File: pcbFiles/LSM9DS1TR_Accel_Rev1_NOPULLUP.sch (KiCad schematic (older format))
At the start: 8 parts

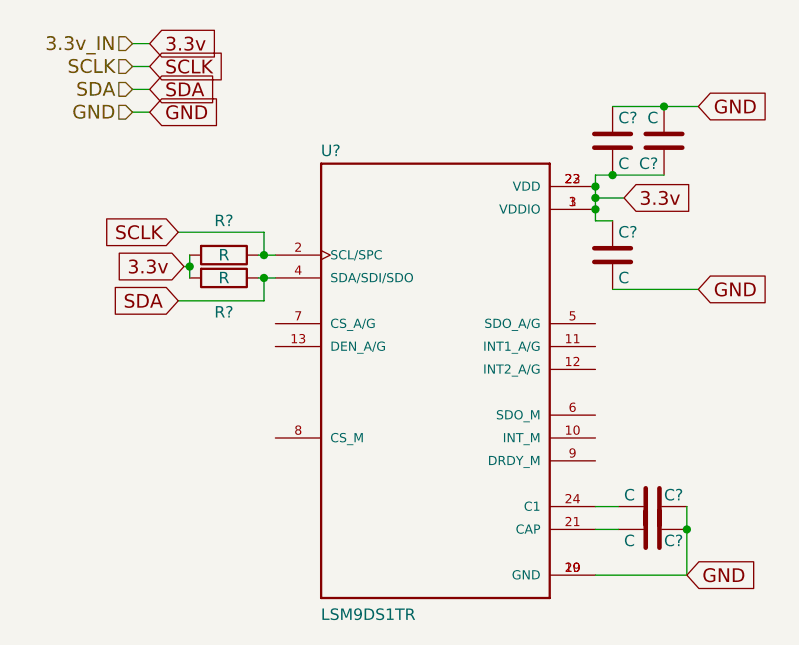
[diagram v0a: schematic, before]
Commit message: Update the circuit schematic
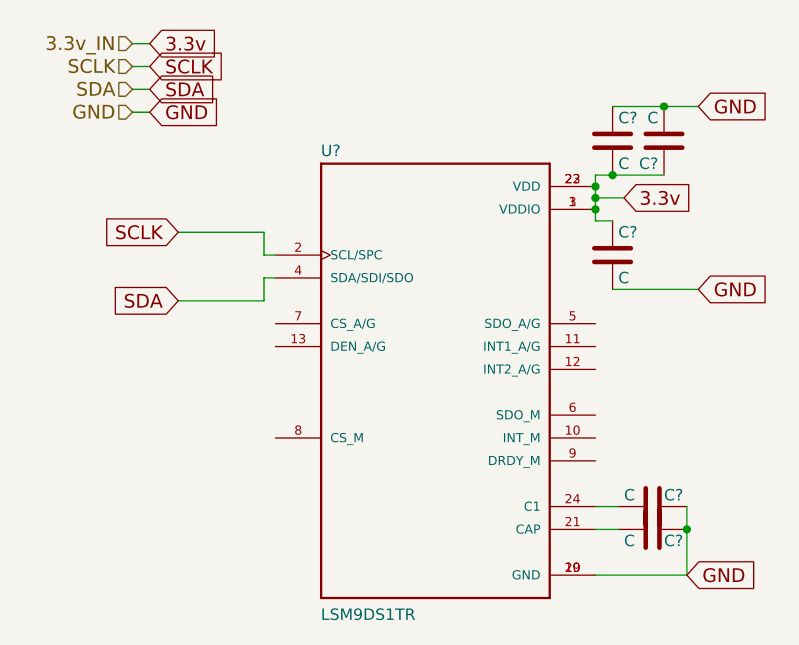
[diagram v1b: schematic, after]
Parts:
- removed R? (x2): R, symbol R
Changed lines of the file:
@@
 $Descr A4 11693 8268
 encoding utf-8
-Sheet 5 7
+Sheet 6 12
 Title ""
 Date ""
@@
 U 1 1 5C4A2352
 P 5375 3325
+AR Path="/5C4A2290/5C4A2352" Ref="U?"  Part="1"
+AR Path="/5C4A8BAE/5C4A2352" Ref="U?"  Part="1"
 F 0 "U?" H 4874 4352 50  0000 L BNN
 F 1 "LSM9DS1TR" H 4874 2323 50  0000 L BNN
@@
 U 1 1 5C4A23DC
 P 6325 3825
+AR Path="/5C4A2290/5C4A23DC" Ref="C?"  Part="1"
+AR Path="/5C4A8BAE/5C4A23DC" Ref="C?"  Part="1"
 F 0 "C?" V 6275 3875 50  0000 L CNN
 F 1 "C" V 6275 3700 50  0000 L CNN
@@
 U 1 1 5C4A24C3
 P 6325 3925
+AR Path="/5C4A2290/5C4A24C3" Ref="C?"  Part="1"
+AR Path="/5C4A8BAE/5C4A24C3" Ref="C?"  Part="1"
 F 0 "C?" V 6375 3975 50  0000 L CNN
 F 1 "C" V 6375 3800 50  0000 L CNN
@@
 U 1 1 5C4A251C
 P 6150 2225
+AR Path="/5C4A2290/5C4A251C" Ref="C?"  Part="1"
+AR Path="/5C4A8BAE/5C4A251C" Ref="C?"  Part="1"
 F 0 "C?" H 6175 2325 50  0000 L CNN
 F 1 "C" H 6175 2125 50  0000 L CNN
@@
 U 1 1 5C4A258F
 P 6375 2225
+AR Path="/5C4A2290/5C4A258F" Ref="C?"  Part="1"
+AR Path="/5C4A8BAE/5C4A258F" Ref="C?"  Part="1"
 F 0 "C?" H 6400 2325 50  0000 L CNN
 F 1 "C" H 6400 2125 50  0000 L CNN
@@
 U 1 1 5C4A25B2
 P 6150 2725
+AR Path="/5C4A2290/5C4A25B2" Ref="C?"  Part="1"
+AR Path="/5C4A8BAE/5C4A25B2" Ref="C?"  Part="1"
 F 0 "C?" H 6175 2825 50  0000 L CNN
 F 1 "C" H 6175 2625 50  0000 L CNN
@@
 	1    0    0    -1
 $EndComp
-$Comp
-L R R?
-U 1 1 5C4A26D9
-P 4450 2725
-F 0 "R?" V 4300 2725 50  0000 C CNN
-F 1 "R" V 4450 2725 50  0000 C CNN
-F 2 "" V 4380 2725 50  0001 C CNN
-F 3 "" H 4450 2725 50  0001 C CNN
-	1    4450 2725
-	0    1    1    0
-$EndComp
-$Comp
-L R R?
-U 1 1 5C4A2742
-P 4450 2825
-F 0 "R?" V 4600 2825 50  0000 C CNN
-F 1 "R" V 4450 2825 50  0000 C CNN
-F 2 "" V 4380 2825 50  0001 C CNN
-F 3 "" H 4450 2825 50  0001 C CNN
-	1    4450 2825
-	0    1    1    0
-$EndComp
-Text GLabel 4275 2775 0    60   Input ~ 0
-3.3v
-Wire Wire Line
-	4300 2725 4300 2825
-Wire Wire Line
-	4300 2775 4275 2775
-Connection ~ 4300 2775
-Wire Wire Line
-	4600 2725 4675 2725
-Wire Wire Line
-	4675 2825 4600 2825
 Text GLabel 4250 2925 0    60   Input ~ 0
 SDA
@@
 Wire Wire Line
 	4625 2625 4625 2725
-Connection ~ 4625 2725
 Wire Wire Line
 	4625 2825 4625 2925
 Wire Wire Line
 	4625 2925 4250 2925
-Connection ~ 4625 2825
 Text GLabel 6200 2475 2    60   Input ~ 0
 3.3v
@@
 Wire Wire Line
 	4125 2100 4050 2100
+Wire Wire Line
+	4625 2725 4675 2725
+Wire Wire Line
+	4625 2825 4675 2825
 $EndSCHEMATC

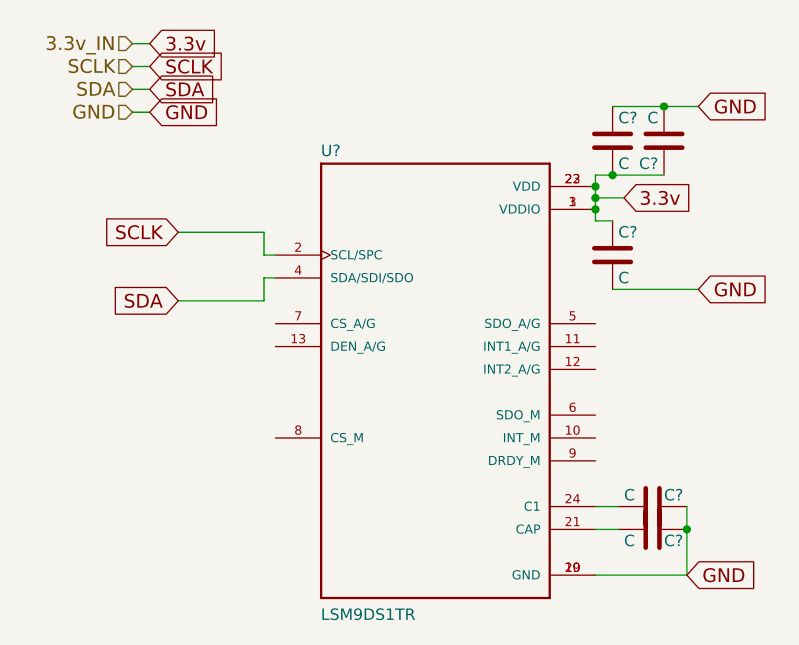
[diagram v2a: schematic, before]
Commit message: Update Footprints and Board Layers
Still need to get foorprint for x... device and the lpf may need to make them if I cannot find them @willcarroll7
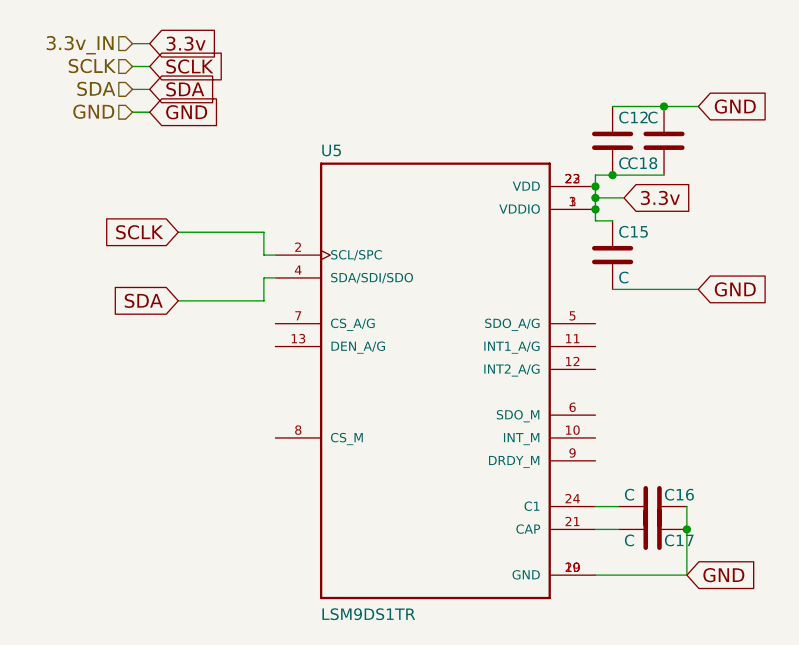
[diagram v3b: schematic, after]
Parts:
- removed C? (x2): C, symbol C
- removed U?: LSM9DS1TR, PQFN43P300X350X102-24N, symbol LSM9DS1TR
- added C15, C17: C, Capacitors_SMD:C_0402, symbol C
- added U5: LSM9DS1TR, LSM9DS1TR:PQFN43P300X350X102-24N, symbol LSM9DS1TR
- C12, C16, C18: renamed from C?; footprint (none) -> Capacitors_SMD:C_0402
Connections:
- net 3.3v: now also C15.1, U5.1 (VDDIO), U5.22 (VDD), U5.23 (VDD), U5.3 (VDDIO)
- net GND: now also C15.2, C17.1, U5.19 (GND), U5.20 (GND)
- net SCLK: now also U5.2 (SCL/SPC)
- net SDA: now also U5.4 (SDA/SDI/SDO)
- net at C16.2: now also U5.24 (C1)
- new net: C17.2, U5.21 (CAP)
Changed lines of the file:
@@
-EESchema Schematic File Version 4
+EESchema Schematic File Version 2
 LIBS:power
+LIBS:device
+LIBS:switches
+LIBS:relays
+LIBS:motors
+LIBS:transistors
+LIBS:conn
+LIBS:linear
+LIBS:regul
 LIBS:74xx
+LIBS:cmos4000
+LIBS:adc-dac
+LIBS:memory
+LIBS:xilinx
+LIBS:microcontrollers
+LIBS:dsp
+LIBS:microchip
+LIBS:analog_switches
+LIBS:motorola
+LIBS:texas
+LIBS:intel
+LIBS:audio
+LIBS:interface
+LIBS:digital-audio
+LIBS:philips
+LIBS:display
+LIBS:cypress
+LIBS:siliconi
+LIBS:opto
+LIBS:atmel
+LIBS:contrib
+LIBS:valves
+LIBS:ADS1115IDGST
+LIBS:CYW20719B1KUMLG
+LIBS:LSM9DS1TR
+LIBS:TPS63001DRCT
+LIBS:MCP73831T-2ACI_OT
+LIBS:A-1JB
+LIBS:XC6119N16A7R-G
 LIBS:GolfGloveMainBoardV1.0.0-cache
-EELAYER 26 0
+EELAYER 25 0
 EELAYER END
 $Descr A4 11693 8268
@@
 $Comp
 L LSM9DS1TR U?
-U 1 1 5C4A2352
+U 1 1 5C59A358
 P 5375 3325
-AR Path="/5C4A2290/5C4A2352" Ref="U?"  Part="1"
-AR Path="/5C4A8BAE/5C4A2352" Ref="U?"  Part="1"
-F 0 "U?" H 4874 4352 50  0000 L BNN
+AR Path="/5C4A2290/5C59A358" Ref="U?"  Part="1"
+AR Path="/5C4A8BAE/5C59A358" Ref="U5"  Part="1"
+F 0 "U5" H 4874 4352 50  0000 L BNN
 F 1 "LSM9DS1TR" H 4874 2323 50  0000 L BNN
-F 2 "PQFN43P300X350X102-24N" H 5375 3325 50  0001 L BNN
+F 2 "LSM9DS1TR:PQFN43P300X350X102-24N" H 5375 3325 50  0001 L BNN
 F 3 "TFLGA-24 STMicroelectronics" H 5375 3325 50  0001 L BNN
 F 4 "LSM9DS1TR" H 5375 3325 50  0001 L BNN "Field4"
@@
 P 6325 3825
 AR Path="/5C4A2290/5C4A23DC" Ref="C?"  Part="1"
-AR Path="/5C4A8BAE/5C4A23DC" Ref="C?"  Part="1"
-F 0 "C?" V 6275 3875 50  0000 L CNN
+AR Path="/5C4A8BAE/5C4A23DC" Ref="C16"  Part="1"
+F 0 "C16" V 6275 3875 50  0000 L CNN
 F 1 "C" V 6275 3700 50  0000 L CNN
-F 2 "" H 6363 3675 50  0001 C CNN
+F 2 "Capacitors_SMD:C_0402" H 6363 3675 50  0001 C CNN
 F 3 "" H 6325 3825 50  0001 C CNN
 	1    6325 3825
@@
 $Comp
 L C C?
-U 1 1 5C4A24C3
+U 1 1 5C59A35A
 P 6325 3925
-AR Path="/5C4A2290/5C4A24C3" Ref="C?"  Part="1"
-AR Path="/5C4A8BAE/5C4A24C3" Ref="C?"  Part="1"
-F 0 "C?" V 6375 3975 50  0000 L CNN
+AR Path="/5C4A2290/5C59A35A" Ref="C?"  Part="1"
+AR Path="/5C4A8BAE/5C59A35A" Ref="C17"  Part="1"
+F 0 "C17" V 6375 3975 50  0000 L CNN
 F 1 "C" V 6375 3800 50  0000 L CNN
-F 2 "" H 6363 3775 50  0001 C CNN
+F 2 "Capacitors_SMD:C_0402" H 6363 3775 50  0001 C CNN
 F 3 "" H 6325 3925 50  0001 C CNN
 	1    6325 3925
@@
 P 6150 2225
 AR Path="/5C4A2290/5C4A251C" Ref="C?"  Part="1"
-AR Path="/5C4A8BAE/5C4A251C" Ref="C?"  Part="1"
-F 0 "C?" H 6175 2325 50  0000 L CNN
+AR Path="/5C4A8BAE/5C4A251C" Ref="C12"  Part="1"
+F 0 "C12" H 6175 2325 50  0000 L CNN
 F 1 "C" H 6175 2125 50  0000 L CNN
-F 2 "" H 6188 2075 50  0001 C CNN
+F 2 "Capacitors_SMD:C_0402" H 6188 2075 50  0001 C CNN
 F 3 "" H 6150 2225 50  0001 C CNN
 	1    6150 2225
@@
 P 6375 2225
 AR Path="/5C4A2290/5C4A258F" Ref="C?"  Part="1"
-AR Path="/5C4A8BAE/5C4A258F" Ref="C?"  Part="1"
-F 0 "C?" H 6400 2325 50  0000 L CNN
+AR Path="/5C4A8BAE/5C4A258F" Ref="C18"  Part="1"
+F 0 "C18" H 6400 2325 50  0000 L CNN
 F 1 "C" H 6400 2125 50  0000 L CNN
-F 2 "" H 6413 2075 50  0001 C CNN
+F 2 "Capacitors_SMD:C_0402" H 6413 2075 50  0001 C CNN
 F 3 "" H 6375 2225 50  0001 C CNN
 	1    6375 2225
@@
 $Comp
 L C C?
-U 1 1 5C4A25B2
+U 1 1 5C59A35D
 P 6150 2725
-AR Path="/5C4A2290/5C4A25B2" Ref="C?"  Part="1"
-AR Path="/5C4A8BAE/5C4A25B2" Ref="C?"  Part="1"
-F 0 "C?" H 6175 2825 50  0000 L CNN
+AR Path="/5C4A2290/5C59A35D" Ref="C?"  Part="1"
+AR Path="/5C4A8BAE/5C59A35D" Ref="C15"  Part="1"
+F 0 "C15" H 6175 2825 50  0000 L CNN
 F 1 "C" H 6175 2625 50  0000 L CNN
-F 2 "" H 6188 2575 50  0001 C CNN
+F 2 "Capacitors_SMD:C_0402" H 6188 2575 50  0001 C CNN
 F 3 "" H 6150 2725 50  0001 C CNN
 	1    6150 2725

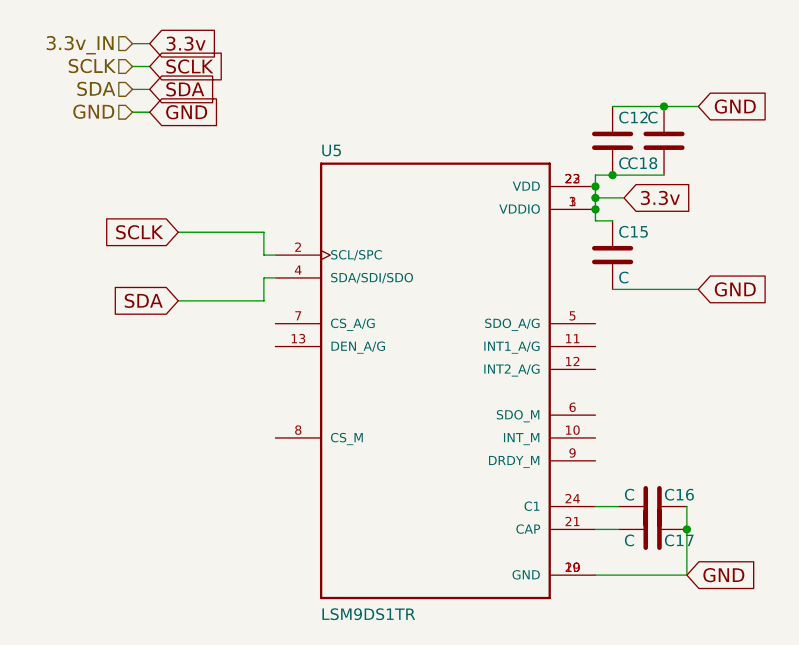
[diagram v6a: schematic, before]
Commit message: Update Board Files
Updated schematic files, completed REV1.0 of the board design, waiting for review by @willcarroll7
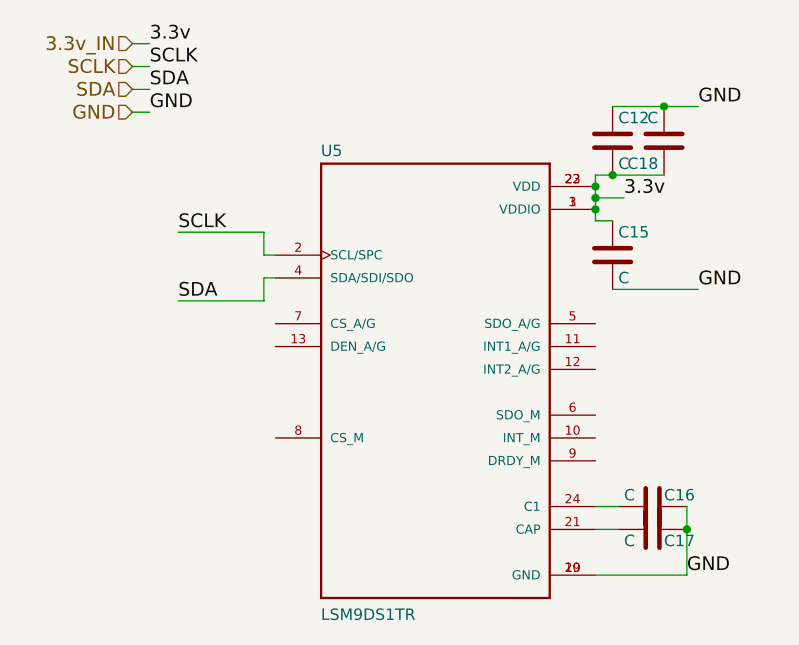
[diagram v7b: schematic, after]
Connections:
- net 3.3v renamed 3.3v_IN
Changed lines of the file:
@@
 LIBS:contrib
 LIBS:valves
-LIBS:2450AT42B100E
-LIBS:A-1JB
 LIBS:ADS1115IDGST
-LIBS:CD4011BM96
 LIBS:CYW20719B1KUMLG
 LIBS:LSM9DS1TR
+LIBS:TPS63001DRCT
 LIBS:MCP73831T-2ACI_OT
+LIBS:A-1JB
+LIBS:XC6119N16A7R-G
+LIBS:2450AT42B100E
+LIBS:CD4011BM96
 LIBS:MMDT3904V-7
 LIBS:MMPQ3904
 LIBS:S2B-PH-K-S_LF__SN_
-LIBS:TPS63001DRCT
-LIBS:XC6119N16A7R-G
 LIBS:GolfGloveMainBoardV1.0.0-cache
 EELAYER 25 0
@@
 	1    0    0    -1
 $EndComp
-Text GLabel 4250 2925 0    60   Input ~ 0
-SDA
-Text GLabel 4250 2625 0    60   Input ~ 0
-SCLK
 Wire Wire Line
 	4250 2625 4625 2625
@@
 Wire Wire Line
 	4625 2925 4250 2925
-Text GLabel 6200 2475 2    60   Input ~ 0
-3.3v
 Wire Wire Line
 	6075 2375 6075 2575
@@
 	6075 2575 6150 2575
 Connection ~ 6075 2525
-Text GLabel 6525 2075 2    60   Input ~ 0
-GND
-Text GLabel 6525 2875 2    60   Input ~ 0
-GND
 Wire Wire Line
 	6150 2075 6525 2075
@@
 Wire Wire Line
 	6150 2875 6525 2875
-Text GLabel 6475 4125 2    60   Input ~ 0
-GND
 Wire Wire Line
 	6475 3825 6475 4125
@@
 Text HLabel 4050 2100 0    60   Input ~ 0
 GND
-Text GLabel 4125 1900 2    60   Input ~ 0
-SCLK
-Text GLabel 4125 2000 2    60   Input ~ 0
-SDA
-Text GLabel 4125 1800 2    60   Input ~ 0
-3.3v
-Text GLabel 4125 2100 2    60   Input ~ 0
-GND
 Wire Wire Line
 	4050 1800 4125 1800
@@
 Wire Wire Line
 	4625 2825 4675 2825
+Text Label 6200 2475 0    60   ~ 0
+3.3v
+Text Label 6525 2075 0    60   ~ 0
+GND
+Text Label 4250 2625 0    60   ~ 0
+SCLK
+Text Label 4250 2925 0    60   ~ 0
+SDA
+Text Label 4125 1900 0    60   ~ 0
+SCLK
+Text Label 4125 2000 0    60   ~ 0
+SDA
+Text Label 4125 1800 0    60   ~ 0
+3.3v
+Text Label 4125 2100 0    60   ~ 0
+GND
+Text Label 6525 2875 0    60   ~ 0
+GND
+Text Label 6475 4125 0    60   ~ 0
+GND
 $EndSCHEMATC

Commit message: Ready For Review
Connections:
- net 3.3v_IN: now also U5.5 (SDO_A/G), U5.6 (SDO_M), U5.7 (CS_A/G), U5.8 (CS_M)
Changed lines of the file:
@@
 Text Label 6475 4125 0    60   ~ 0
 GND
+Text Label 4150 3025 0    60   ~ 0
+3.3v
+Text Label 4150 3500 0    60   ~ 0
+3.3v
+Wire Wire Line
+	4675 3025 4150 3025
+Wire Wire Line
+	4150 3500 4675 3500
+Wire Wire Line
+	4675 3500 4675 3525
+Text Label 6525 3025 0    60   ~ 0
+3.3v
+Text Label 6525 3425 0    60   ~ 0
+3.3v
+Wire Wire Line
+	6075 3025 6525 3025
+Wire Wire Line
+	6075 3425 6525 3425
 $EndSCHEMATC
